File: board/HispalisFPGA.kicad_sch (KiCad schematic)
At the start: 109 parts, among them SW1 SW_DIP_x08

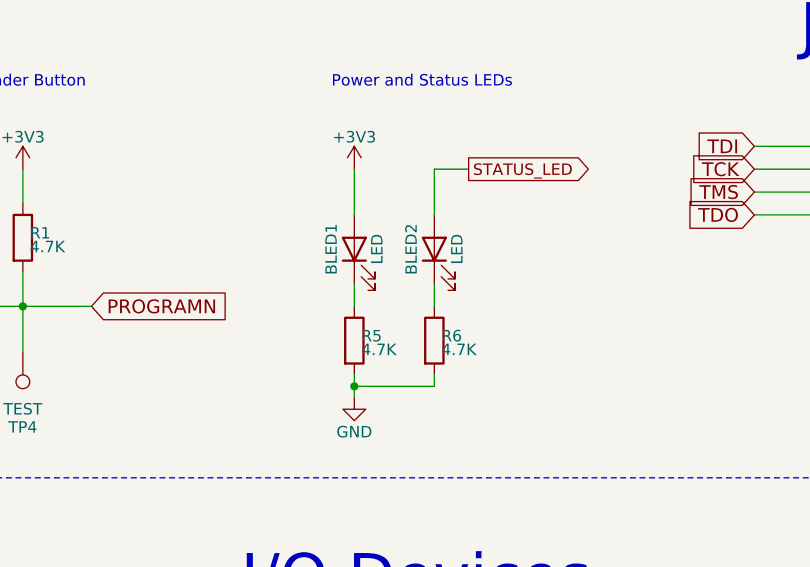
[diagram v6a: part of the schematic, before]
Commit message: Power and status LED correction
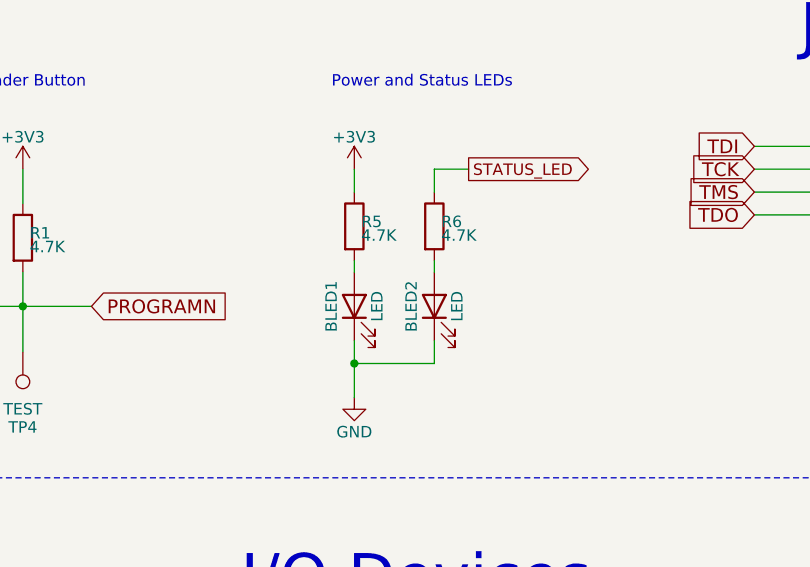
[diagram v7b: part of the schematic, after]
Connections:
- net +3V3: now also R5.1; no longer BLED1.2 (A)
- net GND: now also BLED1.1 (K), BLED2.1 (K); no longer R5.2, R6.2
- net STATUS_LED: now also R6.1; no longer BLED2.2 (A)
- new net: BLED1.2 (A), R5.2
- new net: BLED2.2 (A), R6.2
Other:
- moved on the sheet: BLED1, BLED2, R5, R6
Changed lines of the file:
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@@
 	)
 	(junction
+		(at 264.16 165.1)
+		(diameter 0)
+		(color 0 0 0 0)
+	)
+	(junction
 		(at 165.1 247.65)
 		(diameter 0)
@@
 	)
 	(junction
-		(at 264.16 167.64)
-		(diameter 0)
-		(color 0 0 0 0)
-	)
-	(junction
 		(at 90.17 156.21)
 		(diameter 0)
@@
 	(wire
 		(pts
+			(xy 264.16 162.56) (xy 264.16 165.1)
+		)
+		(stroke
+			(width 0)
+			(type default)
+		)
+	)
+	(wire
+		(pts
 			(xy 83.82 62.23) (xy 80.01 62.23)
 		)
@@
 	(wire
 		(pts
-			(xy 273.05 167.64) (xy 264.16 167.64)
+			(xy 273.05 165.1) (xy 264.16 165.1)
 		)
 		(stroke
@@
 	(wire
 		(pts
-			(xy 273.05 166.37) (xy 273.05 167.64)
-		)
-		(stroke
-			(width 0)
-			(type default)
-		)
-	)
-	(wire
-		(pts
 			(xy 628.65 299.72) (xy 628.65 337.82)
 		)
@@
 	(wire
 		(pts
+			(xy 273.05 162.56) (xy 273.05 165.1)
+		)
+		(stroke
+			(width 0)
+			(type default)
+		)
+	)
+	(wire
+		(pts
 			(xy 209.55 158.75) (xy 209.55 163.83)
 		)
@@
 	(wire
 		(pts
-			(xy 264.16 166.37) (xy 264.16 167.64)
-		)
-		(stroke
-			(width 0)
-			(type default)
-		)
-	)
-	(wire
-		(pts
 			(xy 133.35 290.83) (xy 137.16 290.83)
 		)
@@
 	(wire
 		(pts
-			(xy 264.16 148.59) (xy 264.16 143.51)
-		)
-		(stroke
-			(width 0)
-			(type default)
-		)
-	)
-	(wire
-		(pts
 			(xy 447.04 57.15) (xy 447.04 60.96)
 		)
@@
 	(wire
 		(pts
-			(xy 273.05 148.59) (xy 273.05 143.51)
-		)
-		(stroke
-			(width 0)
-			(type default)
-		)
-	)
-	(wire
-		(pts
 			(xy 245.11 275.59) (xy 245.11 273.05)
 		)
@@
 	(wire
 		(pts
+			(xy 273.05 153.67) (xy 273.05 154.94)
+		)
+		(stroke
+			(width 0)
+			(type default)
+		)
+	)
+	(wire
+		(pts
 			(xy 252.73 55.88) (xy 252.73 58.42)
 		)
@@
 	(wire
 		(pts
+			(xy 273.05 143.51) (xy 273.05 146.05)
+		)
+		(stroke
+			(width 0)
+			(type default)
+		)
+	)
+	(wire
+		(pts
 			(xy 223.52 158.75) (xy 227.33 158.75)
 		)
@@
 	(wire
 		(pts
-			(xy 264.16 156.21) (xy 264.16 158.75)
-		)
-		(stroke
-			(width 0)
-			(type default)
-		)
-	)
-	(wire
-		(pts
 			(xy 115.57 107.95) (xy 115.57 118.11)
 		)
@@
 	(wire
 		(pts
+			(xy 264.16 143.51) (xy 264.16 146.05)
+		)
+		(stroke
+			(width 0)
+			(type default)
+		)
+	)
+	(wire
+		(pts
 			(xy 467.36 219.71) (xy 467.36 254)
 		)
@@
 	(wire
 		(pts
-			(xy 264.16 167.64) (xy 264.16 168.91)
+			(xy 264.16 165.1) (xy 264.16 168.91)
 		)
 		(stroke
@@
 	(wire
 		(pts
+			(xy 264.16 153.67) (xy 264.16 154.94)
+		)
+		(stroke
+			(width 0)
+			(type default)
+		)
+	)
+	(wire
+		(pts
 			(xy 39.37 306.07) (xy 45.72 306.07)
 		)
@@
 	(wire
 		(pts
-			(xy 273.05 156.21) (xy 273.05 158.75)
-		)
-		(stroke
-			(width 0)
-			(type default)
-		)
-	)
-	(wire
-		(pts
 			(xy 245.11 270.51) (xy 245.11 273.05)
 		)
@@
 	(symbol
 		(lib_id "Device:LED")
-		(at 264.16 152.4 90)
+		(at 264.16 158.75 90)
 		(unit 1)
 		(exclude_from_sim no)
@@
 		(dnp no)
 		(property "Reference" "BLED1"
-			(at 261.62 152.4 0)
+			(at 261.62 158.75 0)
 			(effects
 				(font
@@
 		)
 		(property "Value" "LED"
-			(at 266.7 152.4 0)
+			(at 266.7 158.75 0)
 			(effects
 				(font
@@
 		)
 		(property "Footprint" "LED_SMD:LED_0603_1608Metric"
-			(at 264.16 152.4 0)
+			(at 264.16 158.75 0)
 			(effects
 				(font
@@
 		)
 		(property "Datasheet" "https://wmsc.lcsc.com/wmsc/upload/file/pdf/v2/lcsc/1810231112_Hubei-KENTO-Elec-KT-0603R_C2286.pdf"
-			(at 264.16 152.4 0)
+			(at 264.16 158.75 0)
 			(effects
 				(font
@@
 		)
 		(property "Description" ""
-			(at 264.16 152.4 0)
+			(at 264.16 158.75 0)
 			(effects
 				(font
@@
 		)
 		(property "JLC" "0603"
-			(at 264.16 152.4 0)
+			(at 264.16 158.75 0)
 			(effects
 				(font
@@
 		)
 		(property "LCSC" "C2286"
-			(at 264.16 152.4 0)
+			(at 264.16 158.75 0)
 			(effects
 				(font
@@
 	(symbol
 		(lib_id "Device:R")
-		(at 264.16 162.56 0)
+		(at 264.16 149.86 0)
 		(unit 1)
 		(exclude_from_sim no)
@@
 		(dnp no)
 		(property "Reference" "R5"
-			(at 264.922 162.052 0)
+			(at 264.922 149.352 0)
 			(effects
 				(font
@@
 		)
 		(property "Value" "4.7K"
-			(at 264.922 163.576 0)
+			(at 264.922 150.876 0)
 			(effects
 				(font
@@
 		)
 		(property "Footprint" "Resistor_SMD:R_0402_1005Metric"
-			(at 264.16 162.56 0)
+			(at 264.16 149.86 0)
 			(effects
 				(font
@@
 		)
 		(property "Datasheet" ""
-			(at 264.16 162.56 0)
+			(at 264.16 149.86 0)
 			(effects
 				(font
@@
 		)
 		(property "Description" ""
-			(at 264.16 162.56 0)
+			(at 264.16 149.86 0)
 			(effects
 				(font
@@
 		)
 		(property "JLC" "0402"
-			(at 264.16 162.56 0)
+			(at 264.16 149.86 0)
 			(effects
 				(font
@@
 		)
 		(property "LCSC" "C25900"
-			(at 264.16 162.56 0)
+			(at 264.16 149.86 0)
 			(effects
 				(font
@@
 	(symbol
 		(lib_id "Device:R")
-		(at 273.05 162.56 0)
+		(at 273.05 149.86 0)
 		(unit 1)
 		(exclude_from_sim no)
@@
 		(dnp no)
 		(property "Reference" "R6"
-			(at 273.812 162.052 0)
+			(at 273.812 149.352 0)
 			(effects
 				(font
@@
 		)
 		(property "Value" "4.7K"
-			(at 273.812 163.576 0)
+			(at 273.812 150.876 0)
 			(effects
 				(font
@@
 		)
 		(property "Footprint" "Resistor_SMD:R_0402_1005Metric"
-			(at 273.05 162.56 0)
+			(at 273.05 149.86 0)
 			(effects
 				(font
@@
 		)
 		(property "Datasheet" ""
-			(at 273.05 162.56 0)
+			(at 273.05 149.86 0)
 			(effects
 				(font
@@
 		)
 		(property "Description" ""
-			(at 273.05 162.56 0)
+			(at 273.05 149.86 0)
 			(effects
 				(font
@@
 		)
 		(property "JLC" "0402"
-			(at 273.05 162.56 0)
+			(at 273.05 149.86 0)
 			(effects
 				(font
@@
 		)
 		(property "LCSC" "C25900"
-			(at 273.05 162.56 0)
+			(at 273.05 149.86 0)
 			(effects
 				(font
@@
 	(symbol
 		(lib_id "Device:LED")
-		(at 273.05 152.4 90)
+		(at 273.05 158.75 90)
 		(unit 1)
 		(exclude_from_sim no)
@@
 		(dnp no)
 		(property "Reference" "BLED2"
-			(at 270.51 152.4 0)
+			(at 270.51 158.75 0)
 			(effects
 				(font
@@
 		)
 		(property "Value" "LED"
-			(at 275.59 152.4 0)
+			(at 275.59 158.75 0)
 			(effects
 				(font
@@
 		)
 		(property "Footprint" "LED_SMD:LED_0603_1608Metric"
-			(at 273.05 152.4 0)
+			(at 273.05 158.75 0)
 			(effects
 				(font
@@
 		)
 		(property "Datasheet" "https://wmsc.lcsc.com/wmsc/upload/file/pdf/v2/lcsc/1810231112_Hubei-KENTO-Elec-KT-0603R_C2286.pdf"
-			(at 273.05 152.4 0)
+			(at 273.05 158.75 0)
 			(effects
 				(font
@@
 		)
 		(property "Description" ""
-			(at 273.05 152.4 0)
+			(at 273.05 158.75 0)
 			(effects
 				(font
@@
 		)
 		(property "JLC" "0603"
-			(at 273.05 152.4 0)
+			(at 273.05 158.75 0)
 			(effects
 				(font
@@
 		)
 		(property "LCSC" "C2286"
-			(at 273.05 152.4 0)
+			(at 273.05 158.75 0)
 			(effects
 				(font

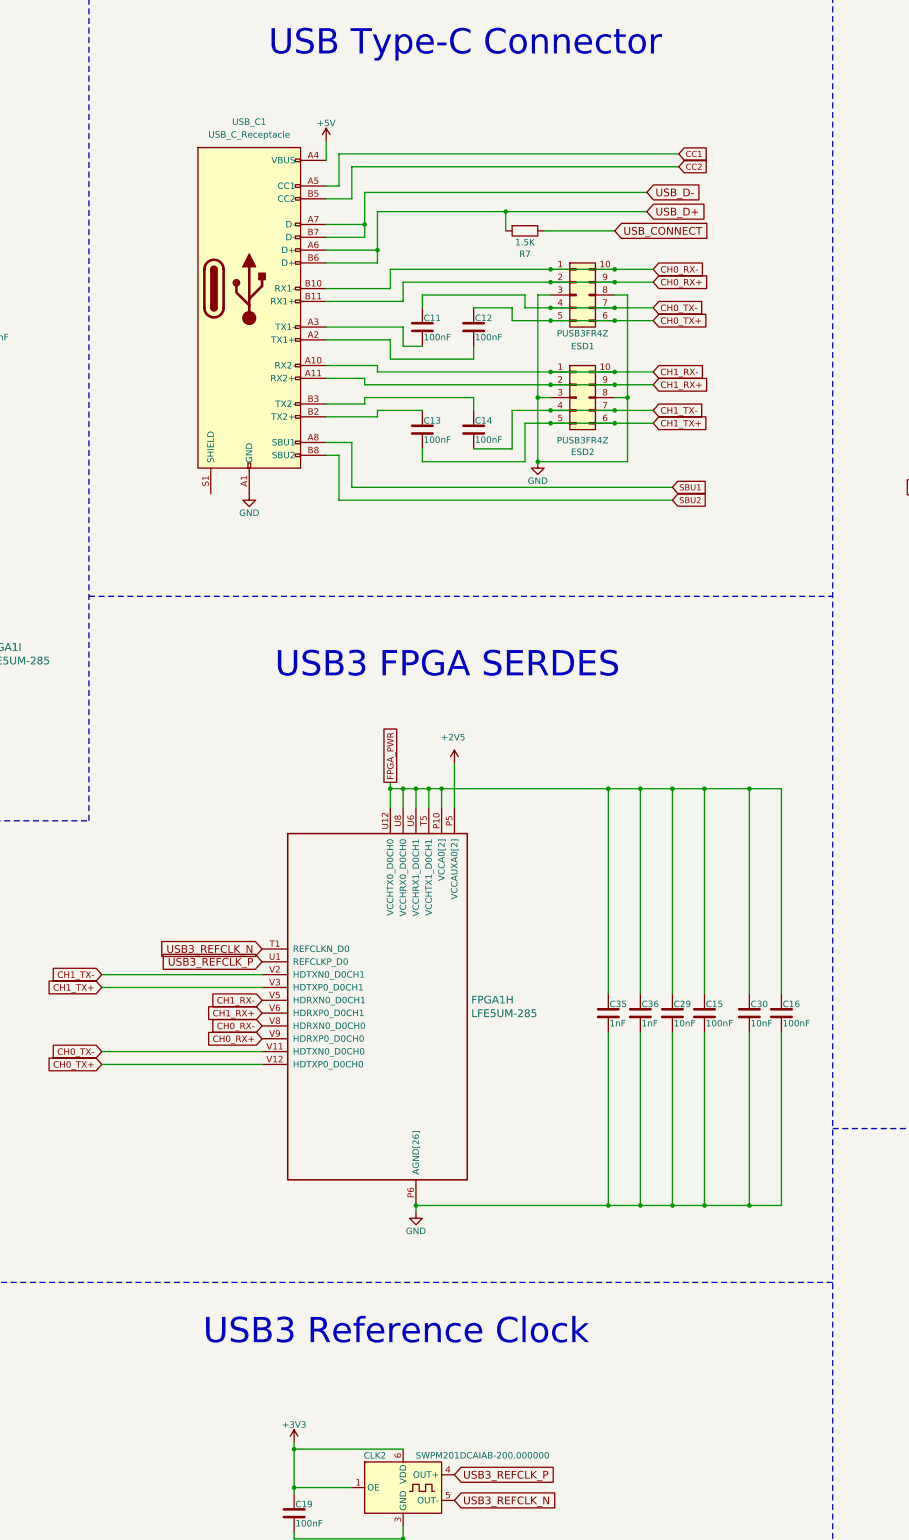
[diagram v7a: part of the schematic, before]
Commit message: Improve USB port protections
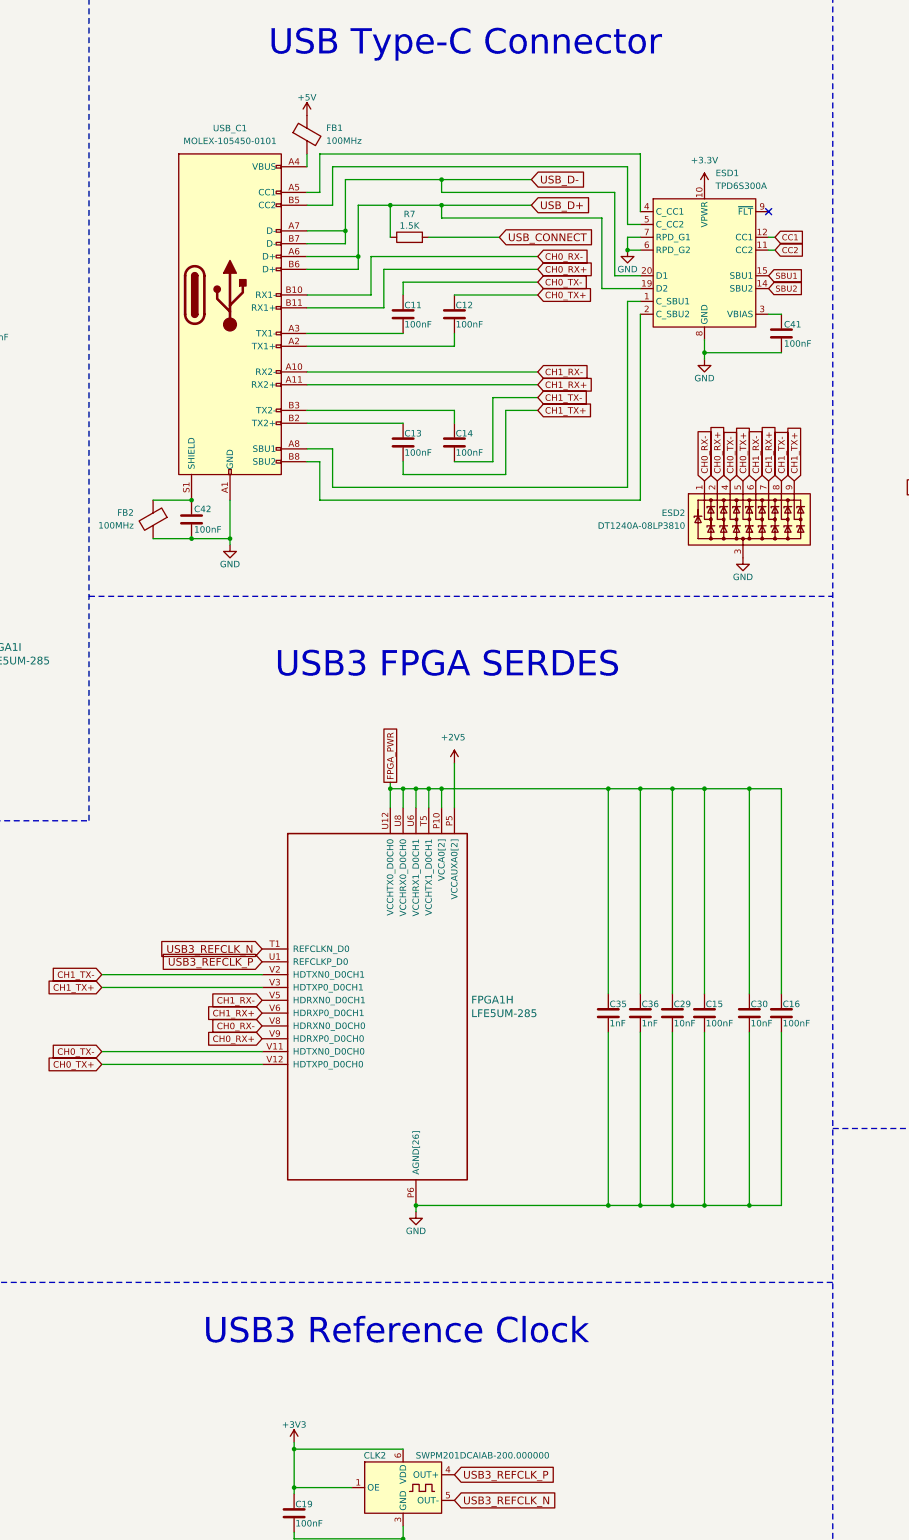
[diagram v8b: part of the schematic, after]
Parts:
- removed ESD1, ESD2: PUSB3FR4Z, Footprints:PUSB3FR4Z, symbol Connector_Generic:Conn_02x05_Counter_Clockwise
- added C41, C42: 100nF, Capacitor_SMD:C_0402_1005Metric, symbol Device:C
- added ESD1: TPD6S300A, Package_DFN_QFN:WQFN-20-1EP_3x3mm_P0.4mm_EP1.7x1.7mm_ThermalVias, symbol Power_Protection:TPD6S300A
- added ESD2: DT1240A-08LP3810, Package_DFN_QFN:UDFN-9_1.0x3.8mm_P0.5mm, symbol Power_Protection:DT1240A-08LP3810
- added FB1, FB2: 100MHz, Inductor_SMD:L_0603_1608Metric, symbol Device:FerriteBead
- USB_C1: value USB_C_Receptacle -> MOLEX-105450-0101; footprint Connector_USB:USB_C_Receptacle_CNCTech_C-ARA1-AK51X -> Connector_USB:USB_C_Receptacle_Molex_105450-0101; LCSC C2927039 -> C134092
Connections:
- net +5V: now also FB1.1; no longer USB_C1.A4 (VBUS), USB_C1.A9 (VBUS), USB_C1.B4 (VBUS), USB_C1.B9 (VBUS)
- net CC1: now also ESD1.12 (CC1); no longer USB_C1.A5 (CC1)
- net CC2: now also ESD1.11 (CC2); no longer USB_C1.B5 (CC2)
- net CH0_RX+: now also ESD2.2 (K2)
- net CH0_RX-: now also ESD2.1 (K1)
- net CH0_TX+: now also ESD2.5 (K4)
- net CH0_TX-: now also ESD2.4 (K3)
- net CH1_RX+: now also ESD2.7 (K6)
- net CH1_RX-: now also ESD2.6 (K5)
- net CH1_TX+: now also ESD2.9 (K8)
- net CH1_TX-: now also ESD2.8 (K7)
- net GND: now also C41.2, C42.2, ESD1.13 (GND), ESD1.16 (GND), ESD1.17 (GND), ESD1.18 (GND), ESD1.21 (GND), ESD1.6 (RPD_G2), ESD1.7 (RPD_G1), ESD1.8 (GND), ESD2.3 (A), FB2.2
- net SBU1: now also ESD1.15 (SBU1); no longer USB_C1.A8 (SBU1)
- net SBU2: now also ESD1.14 (SBU2); no longer USB_C1.B8 (SBU2)
- net USB_CONNECT: now also R7.2; no longer R7.1
- net USB_D+: now also R7.1, ESD1.19 (D2); no longer R7.2
- net USB_D-: now also ESD1.20 (D1)
- net at USB_C1.S1 (SHIELD): now also C42.1, FB2.1
- new net: C41.1, ESD1.3 (VBIAS)
- new net: ESD1.1 (C_SBU1), USB_C1.A8 (SBU1)
- new net: ESD1.2 (C_SBU2), USB_C1.B8 (SBU2)
- new net: ESD1.4 (C_CC1), USB_C1.A5 (CC1)
- new net: ESD1.5 (C_CC2), USB_C1.B5 (CC2)
- new net: FB1.2, USB_C1.A4 (VBUS), USB_C1.A9 (VBUS), USB_C1.B4 (VBUS), USB_C1.B9 (VBUS)
- new net +3.3V: ESD1.10 (VPWR)
- no-connect marks 1 -> 2
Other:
- moved on the sheet: C11, C12, C13, C14, R7, USB_C1
